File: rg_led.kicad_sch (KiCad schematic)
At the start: 7 parts, among them Q100 PJE138K, Q101 PJE138K

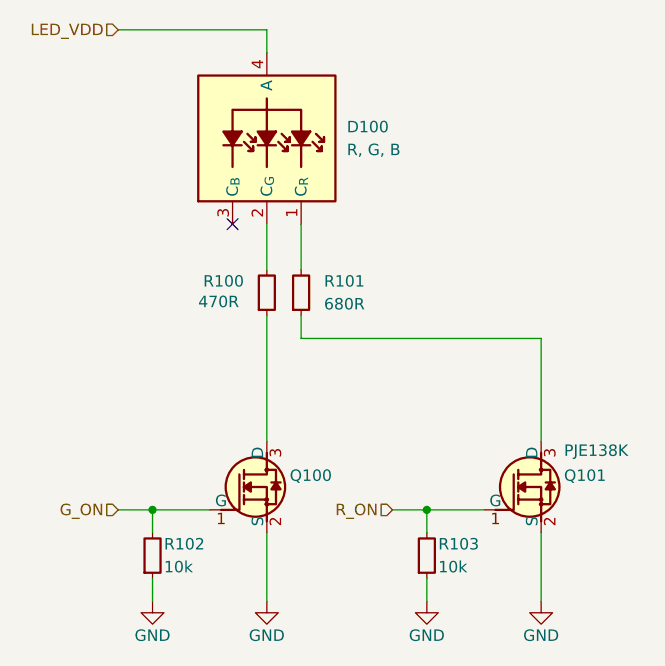
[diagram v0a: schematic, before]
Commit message: [#79468] Update LED resistors
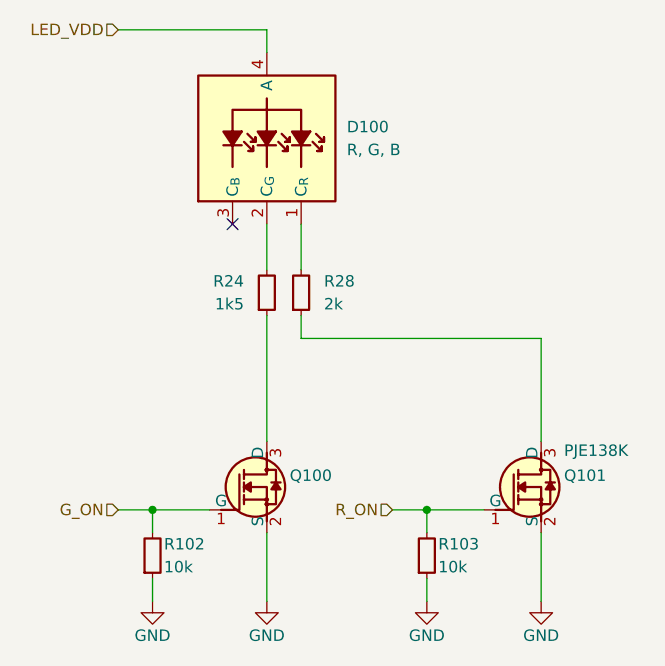
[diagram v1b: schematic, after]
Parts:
- removed R100: R_470R_0402, antmicro-footprints:R_0402_1005Metric, symbol antmicroResistors0402:R_470R_0402
- removed R101: R_680R_0402, antmicro-footprints:R_0402_1005Metric, symbol antmicroResistors0402:R_680R_0402
- added R24: R_1k5_0402, antmicro-footprints:R_0402_1005Metric, symbol antmicroResistors0402:R_1k5_0402
- added R28: R_2k_0402, antmicro-footprints:R_0402_1005Metric, symbol antmicroResistors0402:R_2k_0402
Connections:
- net at Q101.3 (D): now also R28.1
- net at D100.1 (C_{R}): now also R28.2
- net at D100.2 (C_{G}): now also R24.2
- net at Q100.3 (D): now also R24.1
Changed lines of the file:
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@@
+	)
+	(symbol
+		(lib_id "antmicroResistors0402:R_1k5_0402")
+		(at 201.93 143.51 90)
+		(unit 1)
+		(exclude_from_sim no)
+		(in_bom yes)
+		(on_board yes)
+		(dnp no)
+		(property "Reference" "R24"
+			(at 199.39 139.7 90)
+			(effects
+				(font
+					(size 1.27 1.27)
+					(thickness 0.15)
+				)
+				(justify left)
+			)
+		)
+		(property "Value" "R_1k5_0402"
+			(at 214.63 123.19 0)
+			(effects
+				(font
+					(size 1.27 1.27)
+					(thickness 0.15)
+				)
+				(justify left bottom)
+				(hide yes)
+			)
+		)
+		(property "Footprint" "antmicro-footprints:R_0402_1005Metric"
+			(at 217.17 123.19 0)
+			(effects
+				(font
+					(size 1.27 1.27)
+					(thickness 0.15)
+				)
+				(justify left bottom)
+				(hide yes)
+			)
+		)
+		(property "Datasheet" "https://www.bourns.com/docs/product-datasheets/cr.pdf"
+			(at 219.71 123.19 0)
+			(effects
+				(font
+					(size 1.27 1.27)
+					(thickness 0.15)
+				)
+				(justify left bottom)
+				(hide yes)
+			)
+		)
+		(property "Description" "SMD Chip Resistor, 1.5 kohm, ± 1%, 62.5 mW, 0402 [1005 Metric], Thick Film, General Purpose"
+			(at 201.93 143.51 0)
+			(effects
+				(font
+					(size 1.27 1.27)
+				)
+				(hide yes)
+			)
+		)
+		(property "MPN" "CR0402-FX-1501GLF"
+			(at 222.25 123.19 0)
+			(effects
+				(font
+					(size 1.27 1.27)
+					(thickness 0.15)
+				)
+				(justify left bottom)
+				(hide yes)
+			)
+		)
+		(property "Manufacturer" "Bourns"
+			(at 224.79 123.19 0)
+			(effects
+				(font
+					(size 1.27 1.27)
+					(thickness 0.15)
+				)
+				(justify left bottom)
+				(hide yes)
+			)
+		)
+		(property "License" "Apache-2.0"
+			(at 227.33 123.19 0)
+			(effects
+				(font
+					(size 1.27 1.27)
+					(thickness 0.15)
+				)
+				(justify left bottom)
+				(hide yes)
+			)
+		)
+		(property "Author" "Antmicro"
+			(at 229.87 123.19 0)
+			(effects
+				(font
+					(size 1.27 1.27)
+					(thickness 0.15)
+				)
+				(justify left bottom)
+				(hide yes)
+			)
+		)
+		(property "Val" "1k5"
+			(at 199.39 142.24 90)
+			(effects
+				(font
+					(size 1.27 1.27)
+					(thickness 0.15)
+				)
+				(justify left)
+			)
+		)
+		(property "Tolerance" "1%"
+			(at 212.09 123.19 0)
+			(effects
+				(font
+					(size 1.27 1.27)
+				)
+				(justify left bottom)
+				(hide yes)
+			)
+		)
+		(pin "2"
+		)
+		(pin "1"
+		)
+		(instances
+			(project ""
+				(path "/4b393452-b11e-416e-bc83-918ae3cab2f1/0c8eff45-5dcb-4b03-8d03-5bc529aabf64"
+					(reference "R24")
+					(unit 1)
+				)
+				(path "/4b393452-b11e-416e-bc83-918ae3cab2f1/71be9696-f132-4249-a65b-675828057d7e"
+					(reference "R27")
+					(unit 1)
+				)
+				(path "/4b393452-b11e-416e-bc83-918ae3cab2f1/a65537cd-579c-4421-9ceb-eb889d2871a7"
+					(reference "R26")
+					(unit 1)
+				)
+				(path "/4b393452-b11e-416e-bc83-918ae3cab2f1/dec45dd3-d7e6-4fe7-810b-99ab105c3963"
+					(reference "R25")
+					(unit 1)
+				)
+			)
+		)
 	)
 	(symbol
@@
 	)
 	(symbol
-		(lib_id "antmicroResistors0402:R_470R_0402")
-		(at 201.93 143.51 90)
-		(unit 1)
-		(exclude_from_sim no)
-		(in_bom yes)
-		(on_board yes)
-		(dnp no)
-		(property "Reference" "R100"
-			(at 199.39 139.7 90)
-			(do_not_autoplace yes)
-			(effects
-				(font
-					(size 1.27 1.27)
-					(thickness 0.15)
-				)
-				(justify left)
-			)
-		)
-		(property "Value" "R_470R_0402"
-			(at 214.63 123.19 0)
-			(effects
-				(font
-					(size 1.27 1.27)
-					(thickness 0.15)
-				)
-				(justify left bottom)
-				(hide yes)
-			)
-		)
-		(property "Footprint" "antmicro-footprints:R_0402_1005Metric"
-			(at 217.17 123.19 0)
-			(effects
-				(font
-					(size 1.27 1.27)
-					(thickness 0.15)
-				)
-				(justify left bottom)
-				(hide yes)
-			)
-		)
-		(property "Datasheet" "https://www.bourns.com/docs/product-datasheets/cr.pdf"
-			(at 219.71 123.19 0)
-			(effects
-				(font
-					(size 1.27 1.27)
-					(thickness 0.15)
-				)
-				(justify left bottom)
-				(hide yes)
-			)
-		)
-		(property "Description" "SMD Chip Resistor, 470 ohm, ± 1%, 62.5 mW, 0402 [1005 Metric], Thick Film, General Purpose"
-			(at 201.93 143.51 0)
-			(effects
-				(font
-					(size 1.27 1.27)
-				)
-				(hide yes)
-			)
-		)
-		(property "MPN" "CR0402-FX-4700GLF"
-			(at 222.25 123.19 0)
-			(effects
-				(font
-					(size 1.27 1.27)
-					(thickness 0.15)
-				)
-				(justify left bottom)
-				(hide yes)
-			)
-		)
-		(property "Manufacturer" "Bourns"
-			(at 224.79 123.19 0)
-			(effects
-				(font
-					(size 1.27 1.27)
-					(thickness 0.15)
-				)
-				(justify left bottom)
-				(hide yes)
-			)
-		)
-		(property "License" "Apache-2.0"
-			(at 227.33 123.19 0)
-			(effects
-				(font
-					(size 1.27 1.27)
-					(thickness 0.15)
-				)
-				(justify left bottom)
-				(hide yes)
-			)
-		)
-		(property "Author" "Antmicro"
-			(at 229.87 123.19 0)
-			(effects
-				(font
-					(size 1.27 1.27)
-					(thickness 0.15)
-				)
-				(justify left bottom)
-				(hide yes)
-			)
-		)
-		(property "Val" "470R"
-			(at 194.31 141.986 90)
-			(effects
-				(font
-					(size 1.27 1.27)
-					(thickness 0.15)
-				)
-				(justify right)
-			)
-		)
-		(property "Tolerance" "1%"
-			(at 212.09 123.19 0)
-			(effects
-				(font
-					(size 1.27 1.27)
-				)
-				(justify left bottom)
-				(hide yes)
-			)
-		)
-		(pin "1"
-		)
-		(pin "2"
-		)
-		(instances
-			(project ""
-				(path "/4b393452-b11e-416e-bc83-918ae3cab2f1/0c8eff45-5dcb-4b03-8d03-5bc529aabf64"
-					(reference "R100")
-					(unit 1)
-				)
-				(path "/4b393452-b11e-416e-bc83-918ae3cab2f1/71be9696-f132-4249-a65b-675828057d7e"
-					(reference "R400")
-					(unit 1)
-				)
-				(path "/4b393452-b11e-416e-bc83-918ae3cab2f1/a65537cd-579c-4421-9ceb-eb889d2871a7"
-					(reference "R300")
-					(unit 1)
-				)
-				(path "/4b393452-b11e-416e-bc83-918ae3cab2f1/dec45dd3-d7e6-4fe7-810b-99ab105c3963"
-					(reference "R200")
-					(unit 1)
-				)
-			)
-		)
-	)
-	(symbol
 		(lib_id "antmicropower:GND")
 		(at 219.71 175.26 0)
@@
 	)
 	(symbol
-		(lib_id "antmicroResistors0402:R_680R_0402")
+		(lib_id "antmicroResistors0402:R_2k_0402")
 		(at 205.74 143.51 90)
 		(unit 1)
@@
 		(dnp no)
 		(fields_autoplaced yes)
-		(property "Reference" "R101"
+		(property "Reference" "R28"
 			(at 208.28 139.7 90)
 			(effects
@@
 			)
 		)
-		(property "Value" "R_680R_0402"
+		(property "Value" "R_2k_0402"
 			(at 218.44 123.19 0)
 			(effects
@@
 			)
 		)
-		(property "Description" "SMD Chip Resistor, 680 ohm, ± 1%, 63 mW, 0402 [1005 Metric], Thick Film, General Purpose"
+		(property "Description" "SMD Chip Resistor, 2 kohm, ± 1%, 62.5 mW, 0402 [1005 Metric], Thick Film, General Purpose"
 			(at 205.74 143.51 0)
 			(effects
@@
 			)
 		)
-		(property "MPN" "CR0402-FX-6800GLF"
+		(property "MPN" "CR0402-FX-2001GLF"
 			(at 226.06 123.19 0)
 			(effects
@@
 			)
 		)
-		(property "Val" "680R"
+		(property "Val" "2k"
 			(at 208.28 142.24 90)
 			(effects
@@
 			(project ""
 				(path "/4b393452-b11e-416e-bc83-918ae3cab2f1/0c8eff45-5dcb-4b03-8d03-5bc529aabf64"
-					(reference "R101")
+					(reference "R28")
 					(unit 1)
 				)
 				(path "/4b393452-b11e-416e-bc83-918ae3cab2f1/71be9696-f132-4249-a65b-675828057d7e"
-					(reference "R401")
+					(reference "R31")
 					(unit 1)
 				)
 				(path "/4b393452-b11e-416e-bc83-918ae3cab2f1/a65537cd-579c-4421-9ceb-eb889d2871a7"
-					(reference "R301")
+					(reference "R30")
 					(unit 1)
 				)
 				(path "/4b393452-b11e-416e-bc83-918ae3cab2f1/dec45dd3-d7e6-4fe7-810b-99ab105c3963"
-					(reference "R201")
-					(unit 1)
-				)
+					(reference "R29")
+					(unit 1)
+				)

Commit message: [#79620] Rename to JOB ICT Bottom Board, Bump rev to 1.1.1
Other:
- title: Jetson Orin Baseboard Test Rig -> Jetson Orin Baseboard ICT Bottom Board
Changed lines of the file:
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@@
 	(paper "A3")
 	(title_block
-		(title "Jetson Orin Baseboard Test Rig")
-		(date "2025-06-25")
-		(rev "1.1.0")
+		(title "Jetson Orin Baseboard ICT Bottom Board")
+		(date "2025-07-01")
+		(rev "1.1.1")
 		(company "Antmicro Ltd")
 		(comment 1 "www.antmicro.com")
